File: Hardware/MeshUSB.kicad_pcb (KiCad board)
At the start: 2 copper layers, 30.2 x 44.3 mm, 43 parts, among them P1 USB_4, P2 PVCell, P30 JST_2, Q1 MOS_P, Q2 MOS_P-INFINEON-BSS83P, U1 XBEE, U2 AP7313-3.3VREGULATOR, U4 FT231X-SSOP, U5 LTC4070

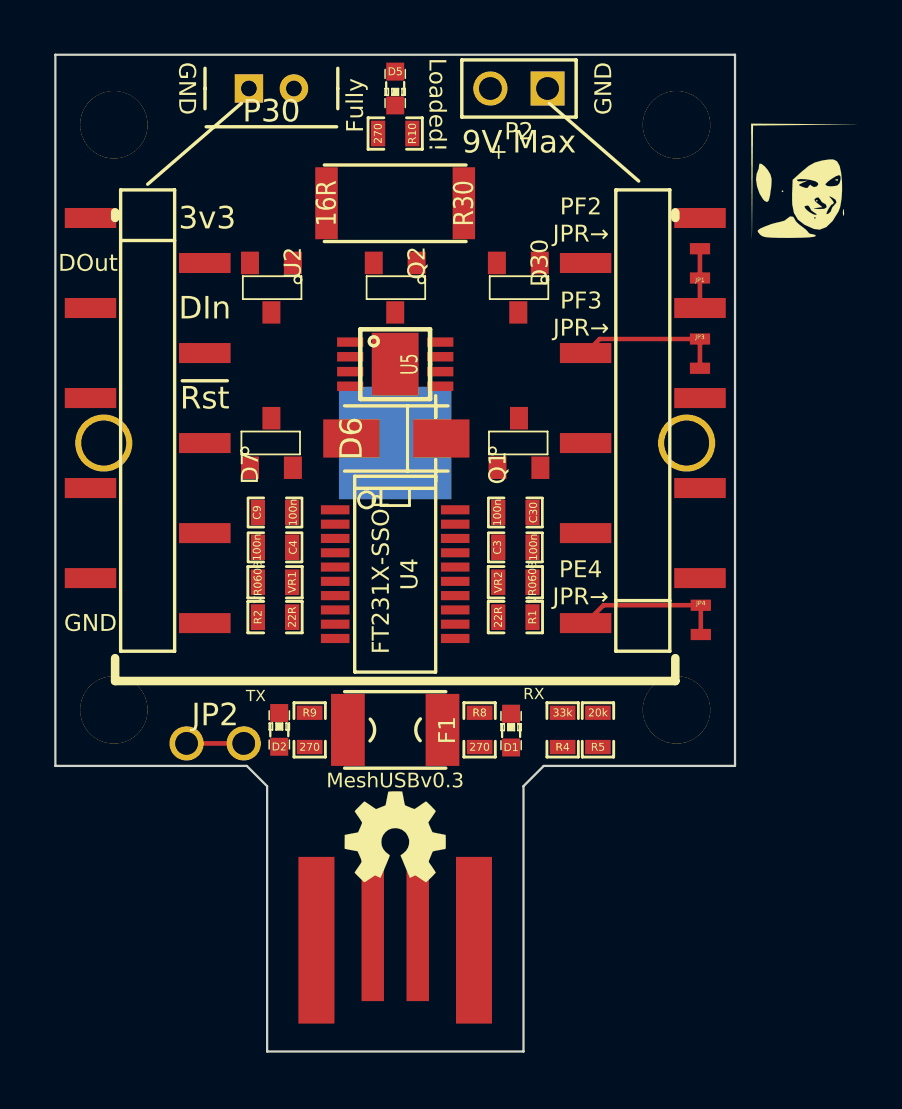
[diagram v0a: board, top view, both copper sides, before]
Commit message: Routed. In need of further review and a few more TODOs.
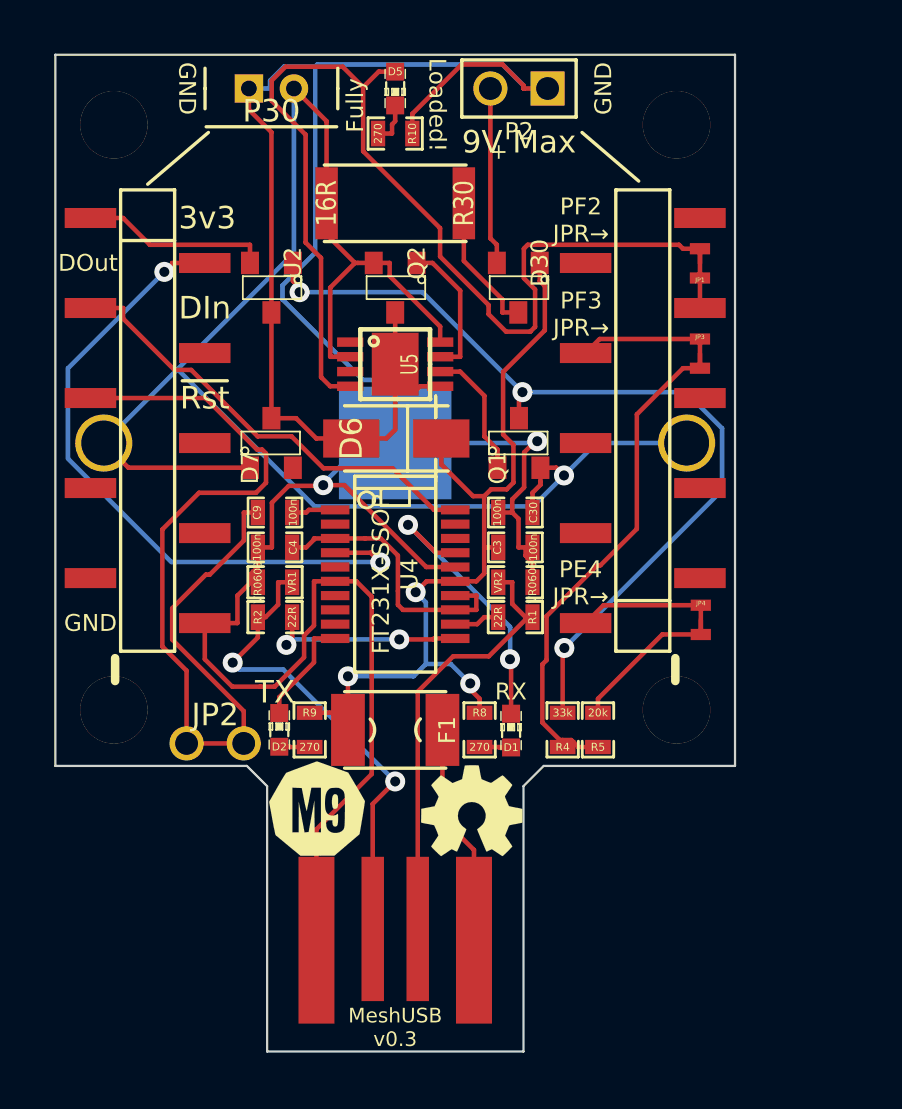
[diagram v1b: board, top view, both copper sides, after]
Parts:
- added VAL: M9Logo-scaled, _M9_LOGO_:M9Logo-scaled, F.Cu at (145.1, 131.3)
- G0: moved to B.Cu
- JP1: footprint _MUSB_SMTJumper -> _MUSB_:_MUSB_SMTJumper
- moved G0 37.6 mm to (148.5, 136.3)
- moved G1 3.59 mm to (151.9, 131.3)
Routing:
- net GND: track 0.00 -> 138.4 mm, vias 0 -> 2
- net Net-(C30-Pad1): track 0.00 -> 76.2 mm, vias 0 -> 1
- net _MT_PF2: track 1.33 -> 50.5 mm
- net Net-(Q1-Pad3): track 0.00 -> 39.5 mm, vias 0 -> 3
- net USB_VDD: track 0.00 -> 38.4 mm, vias 0 -> 3
- net Net-(H1-Pad2): track 0.00 -> 30.0 mm, vias 0 -> 2
- net Net-(H1-Pad5): track 0.00 -> 25.5 mm
- net _MT_PF3: track 0.00 -> 23.0 mm
- net Net-(P1-Pad2): track 0.00 -> 21.6 mm, vias 0 -> 2
- net Net-(H1-Pad3): track 0.00 -> 20.2 mm
- net Net-(P1-Pad3): track 0.00 -> 19.5 mm
- net Net-(C9-Pad1): track 0.00 -> 13.6 mm
- net Net-(D1-Pad2): track 0.00 -> 12.9 mm, vias 0 -> 2
- net VCCIO: track 0.00 -> 12.6 mm
- net Net-(F1-Pad1): track 0.00 -> 9.93 mm
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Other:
- board text added: "MeshUSB v0.3"
- board text added: "by Robert Powers"
- board text added: "©M9Design.co 2013 OpenHardware Under TAPR OHL tapr.org/OHL"
- board text removed: "MeshUSBv0.3"
- board text removed: "©BobPowers 2013 OpenHardware Under TAPR OHL tapr.org/OHL"

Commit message: Layout & routing nearly final. Current carrying trace widths need to be embiggened.
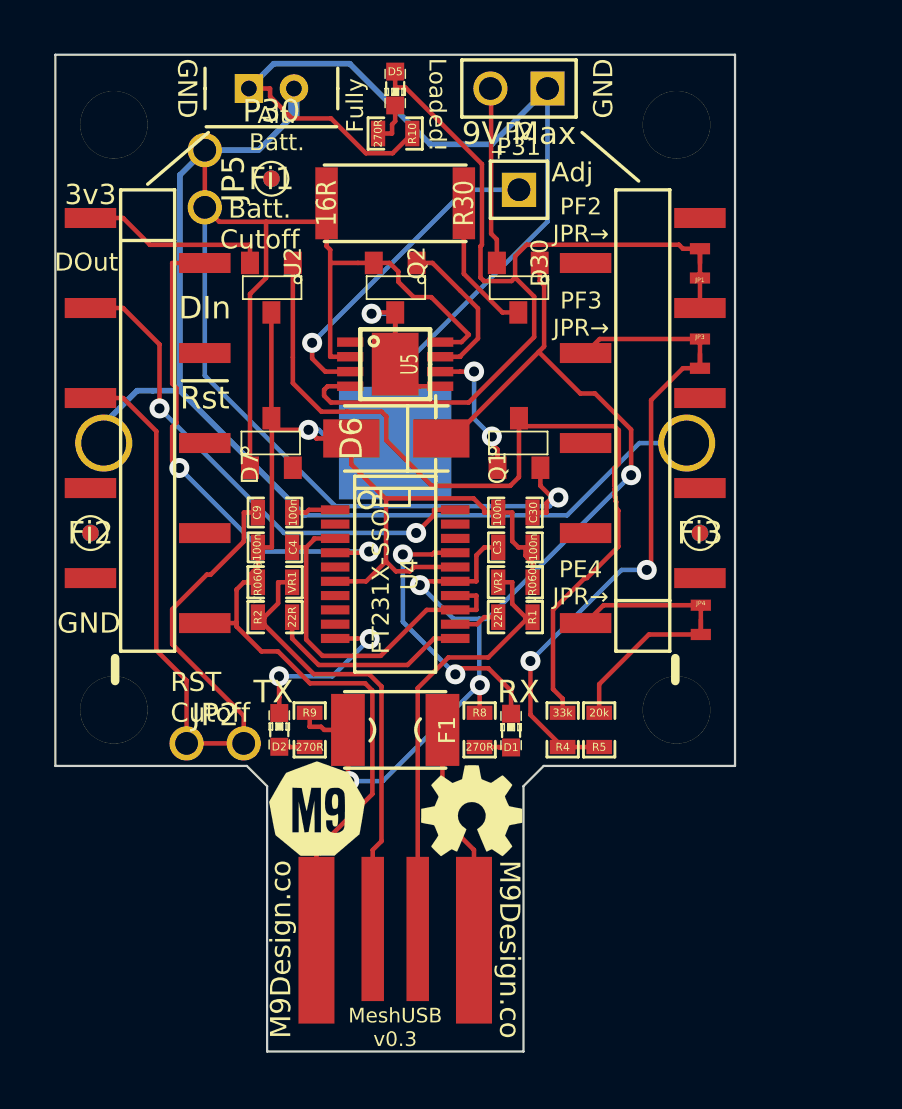
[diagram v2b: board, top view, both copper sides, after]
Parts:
- added Fi1: CONN_1, _MUSB_:_MUSB_Fiducial, F.Cu at (143.0, 103.3)
- added Fi2: CONN_1, _MUSB_:_MUSB_Fiducial, F.Cu at (135.0, 119.0)
- added Fi3: CONN_1, _MUSB_:_MUSB_Fiducial, F.Cu at (162.0, 119.0)
- added JP5: CONN_TH_JMPR_DEFAULTCLOSED, _MUSB_:_MUSB_TH-Jumper_Default-Connected, F.Cu at (140.0, 103.3)
- added P31: CONN_1, Pin_Arrays:PIN_ARRAY_1, F.Cu at (154.0, 103.8)
- R10, R8, R9: value 270 -> 270R
- moved R5 0.05 mm to (157.6, 127.8)
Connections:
- Li-Battery1 pad 1: Net-(C30-Pad1) -> Net-(JP5-Pad2)
- P30 pad 2: Net-(C30-Pad1) -> Net-(JP5-Pad2)
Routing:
- net Net-(JP5-Pad2): track 0.00 -> 47.9 mm
- net GND: track 138.4 -> 119.3 mm
- net Net-(P31-Pad1): track 0.00 -> 14.6 mm, vias 0 -> 1
- net Net-(C30-Pad1): track 76.2 -> 62.8 mm
- net USB_VDD: track 38.4 -> 51.5 mm, vias 3 -> 4
- net _MT_PF2: track 50.5 -> 39.3 mm
- net Net-(H1-Pad2): track 30.0 -> 22.4 mm
- net Net-(H1-Pad5): track 25.5 -> 18.0 mm
- net VCCIO: track 12.6 -> 16.5 mm
- net Net-(D2-Pad2): track 4.89 -> 7.89 mm, vias 0 -> 2
- net Net-(H1-Pad3): track 20.2 -> 22.6 mm, vias 0 -> 2
- net Net-(P1-Pad2): track 21.6 -> 20.3 mm, vias 2 -> 0
- net _MT_PF3: track 23.0 -> 23.9 mm, vias 0 -> 2
- net Net-(Q2-Pad1): track 6.27 -> 6.93 mm
- net _MT_PE4: track 7.03 -> 7.56 mm
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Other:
- net class 10thou added: clearance 0.2032, trace_width 0.254, via_dia 0.889, via_drill 0.635
- net class 20thou added: clearance 0.2032, trace_width 0.508, via_dia 0.889, via_drill 0.635
- board text added: "Adj"
- board text added: "Alt. Batt."
- board text added: "Batt. Cutoff"
- board text added: "M9Design.co"
- board text added: "RST Cutoff"

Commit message: Adding nets.
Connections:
- net Net-(C30-Pad1) renamed /Charge+
- net Net-(D30-Pad2) renamed /PV+
- net Net-(D30-Pad3) renamed /CC1
- net Net-(F1-Pad1) renamed /USBPwrIn
- net Net-(JP5-Pad2) renamed /BatConn+

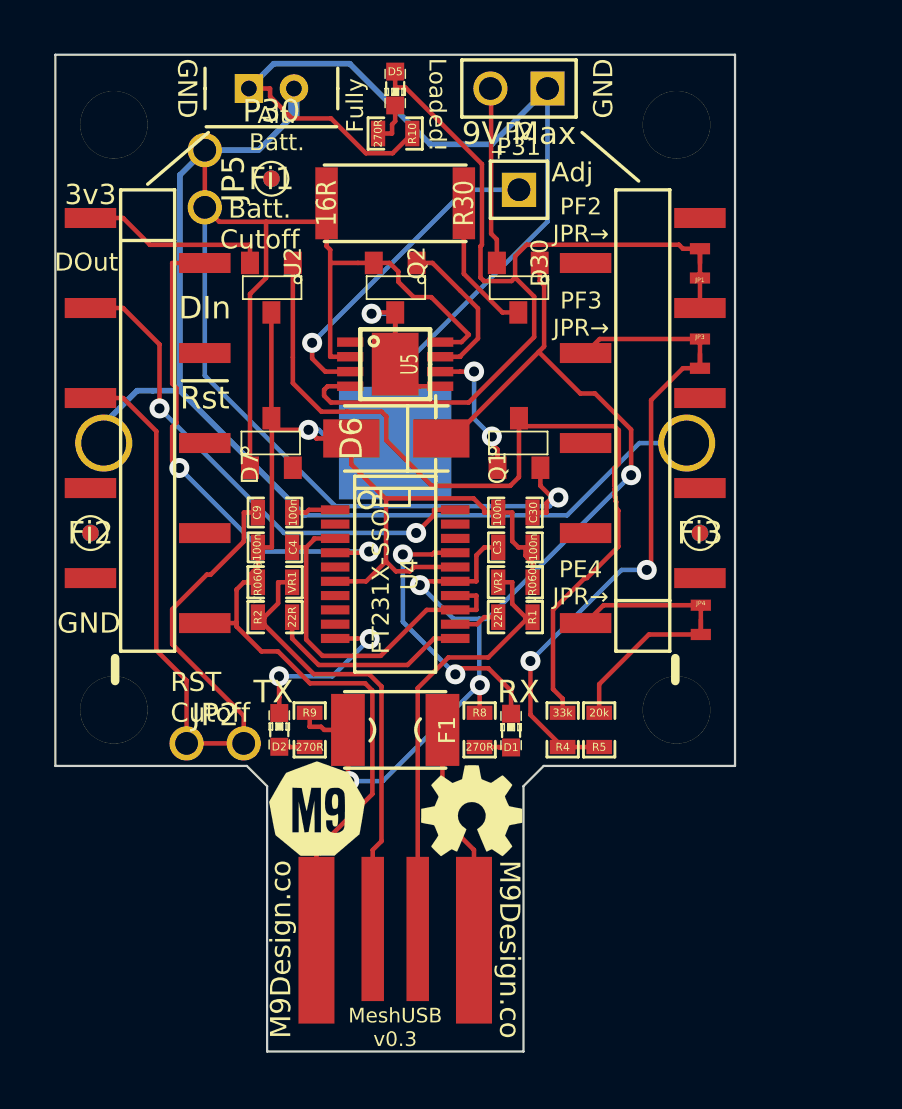
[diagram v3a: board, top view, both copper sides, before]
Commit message: Embiggining and reroute done. Double checks on pad-connect traces and via placements next.
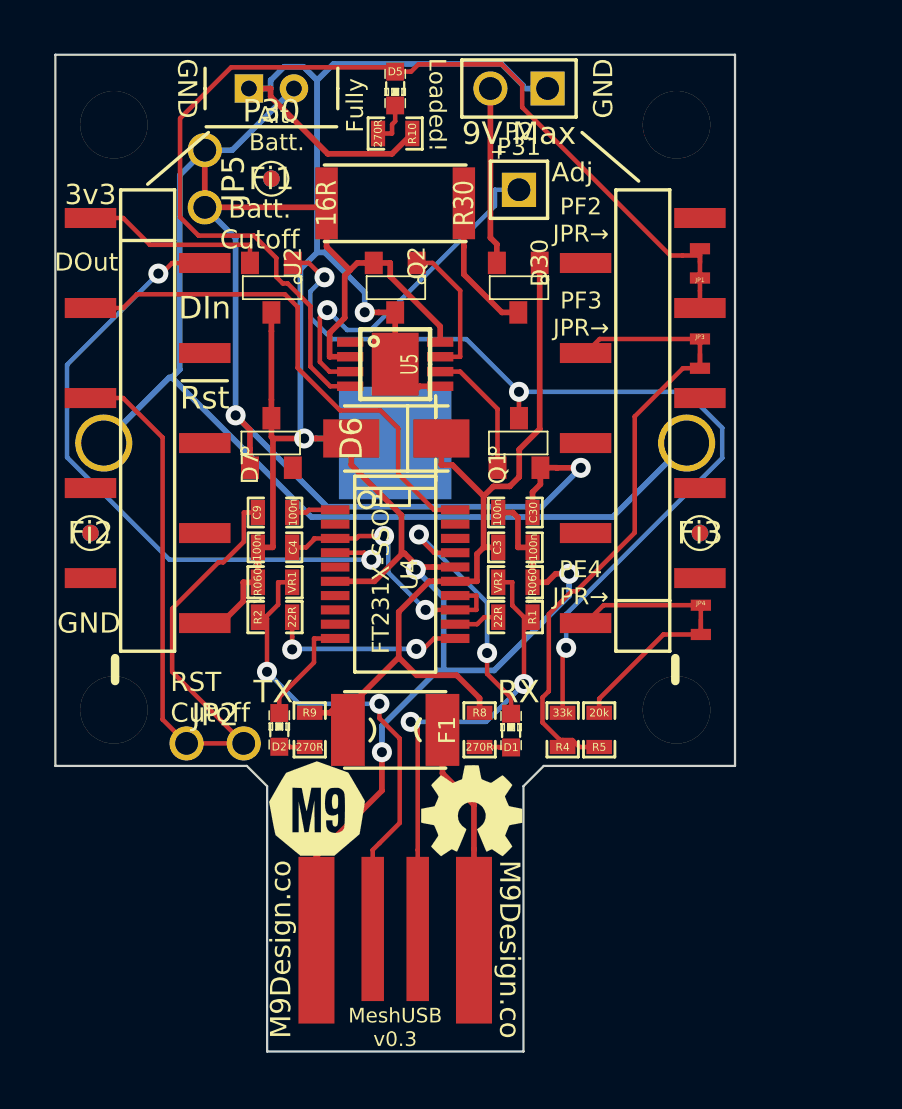
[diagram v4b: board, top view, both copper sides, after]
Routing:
- net USB_VDD: track 51.5 -> 37.0 mm, vias 4 -> 0
- net /Charge+: track 62.8 -> 54.5 mm, vias 1 -> 2
- net _MT_PF2: track 39.3 -> 46.8 mm
- net Net-(H1-Pad2): track 22.4 -> 29.3 mm
- net VCCIO: track 16.5 -> 12.2 mm, vias 0 -> 2
- net Net-(D2-Pad2): track 7.89 -> 4.89 mm, vias 2 -> 0
- net GND: track 119.3 -> 120.8 mm, vias 2 -> 5
- net Net-(Q1-Pad3): track 39.3 -> 40.8 mm, vias 0 -> 3
- net /BatConn+: track 47.9 -> 49.4 mm
- net Net-(P1-Pad2): track 20.3 -> 21.7 mm, vias 0 -> 2
- net Net-(P31-Pad1): track 14.6 -> 15.8 mm
- net Net-(P1-Pad3): track 19.6 -> 20.8 mm, vias 0 -> 2
- net Net-(D1-Pad2): track 12.7 -> 11.7 mm
- net _MT_PF3: track 23.9 -> 23.1 mm, vias 2 -> 0
- net Net-(H2-Pad8): track 0.00 -> 0.76 mm
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
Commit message: Final touches, render, update some datasheets.
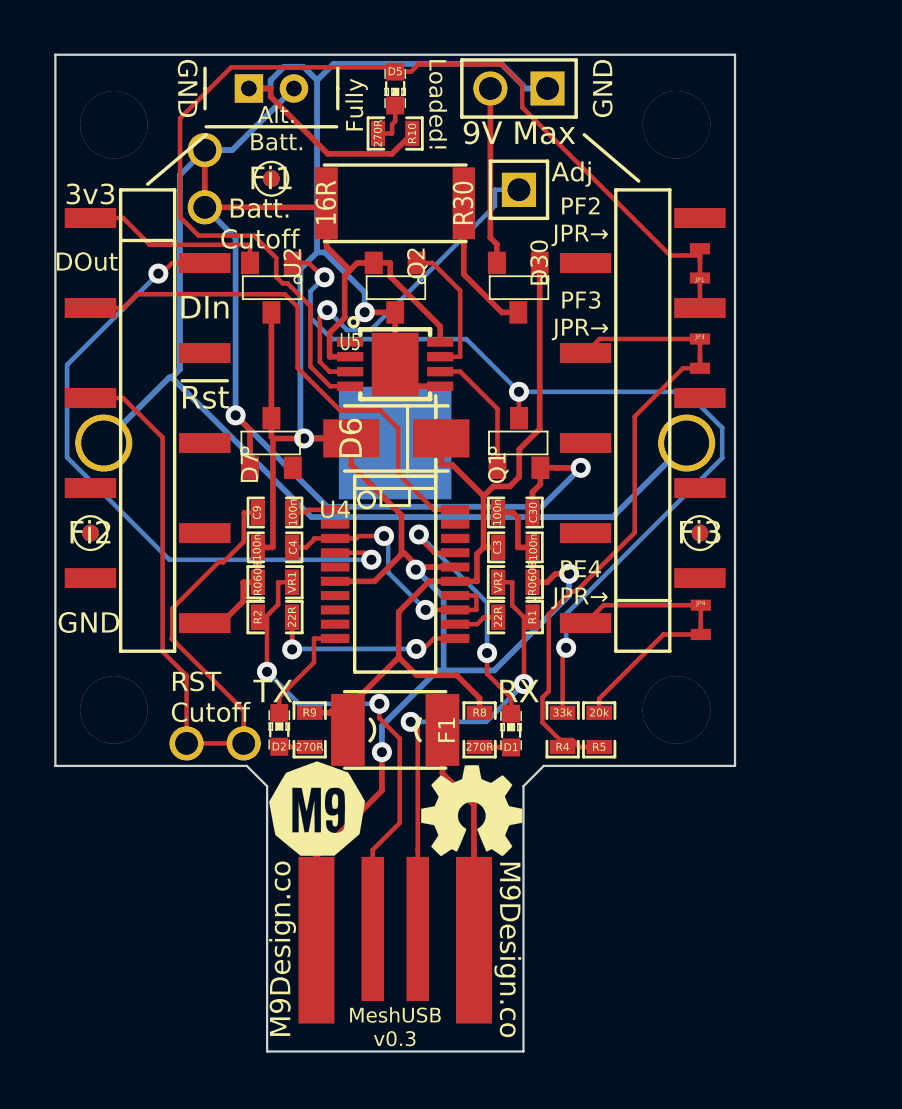
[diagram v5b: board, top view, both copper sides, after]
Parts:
- U1: footprint _MUSB_XBee_Board_OUTLINE_ONLY -> _MUSB_:_MUSB_XBee_Board_OUTLINE_ONLY
- U4: footprint _MUSB_SSOP20-FT231X -> _MUSB_:_MUSB_SSOP20-FT231X
- U5: footprint SSOP8-9 -> _MUSB_:_MUSB_SSOP8-9

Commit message: V0.3 Production ready. This version sent for quote. TODO: Placements.
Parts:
- P1: footprint _MUSB_USB-A-PCB -> _MUSB_:_MUSB_USB-A-PCB
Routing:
- net GND: track 120.8 -> 121.6 mm
- net _MT_PE4: track 6.97 -> 7.66 mm
- net Net-(P1-Pad3): track 20.8 -> 21.4 mm

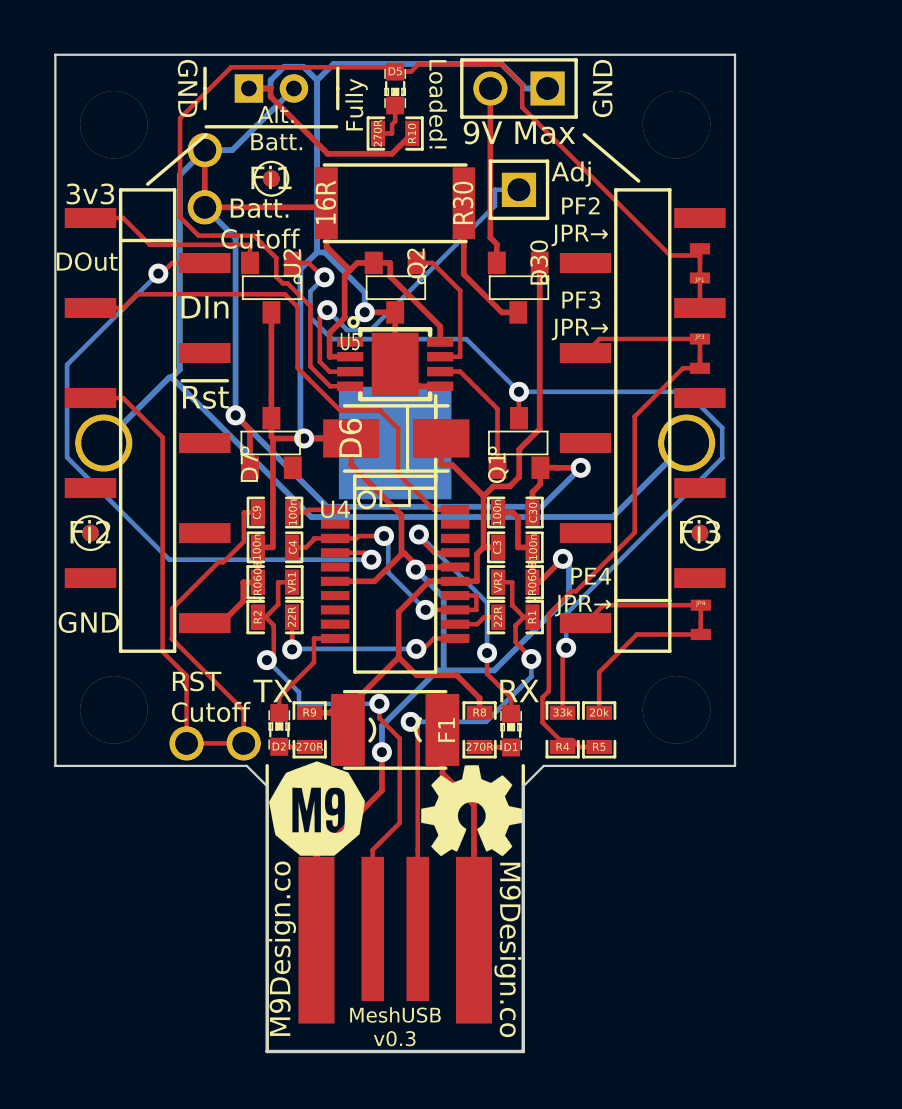
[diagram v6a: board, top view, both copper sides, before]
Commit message: Positions and minor silk.
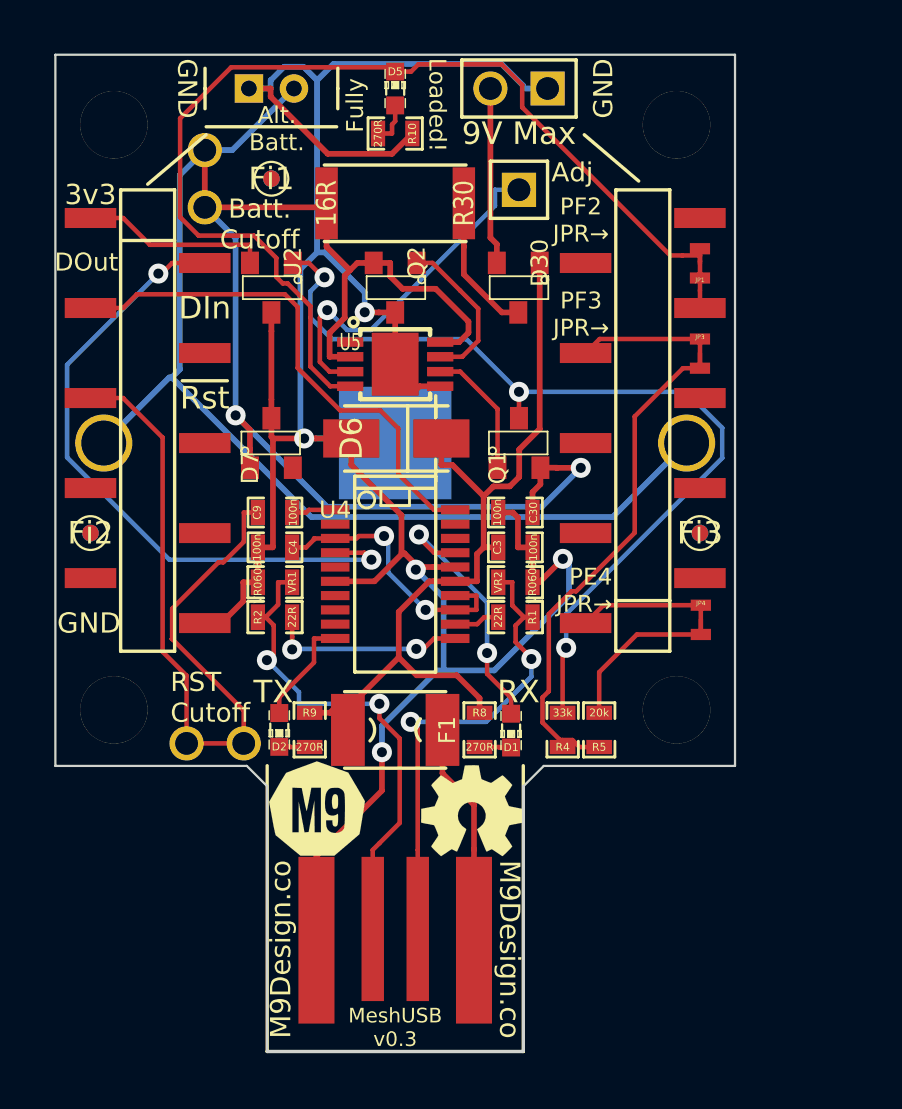
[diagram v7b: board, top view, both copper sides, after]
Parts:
- D1, D2, D5: footprint _MUSB_LED-0603 -> _MUSB_:_MUSB_LED-0603
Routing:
- net /Charge+: track 54.5 -> 56.9 mm
- net Net-(Q2-Pad1): track 6.27 -> 6.99 mm
